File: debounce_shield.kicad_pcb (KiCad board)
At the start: 2 copper layers, 65 x 56 mm, 75 parts, among them IC1 LTV-814, IC2 LTV-814, IC3 LTV-814, IC4 LTV-814, IC5 LTV-814, IC6 LTV-814, IC7 MAX16914AUB+, J1 Conn_01x06, J2 RPi_GPIO, J3 Conn_01x06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

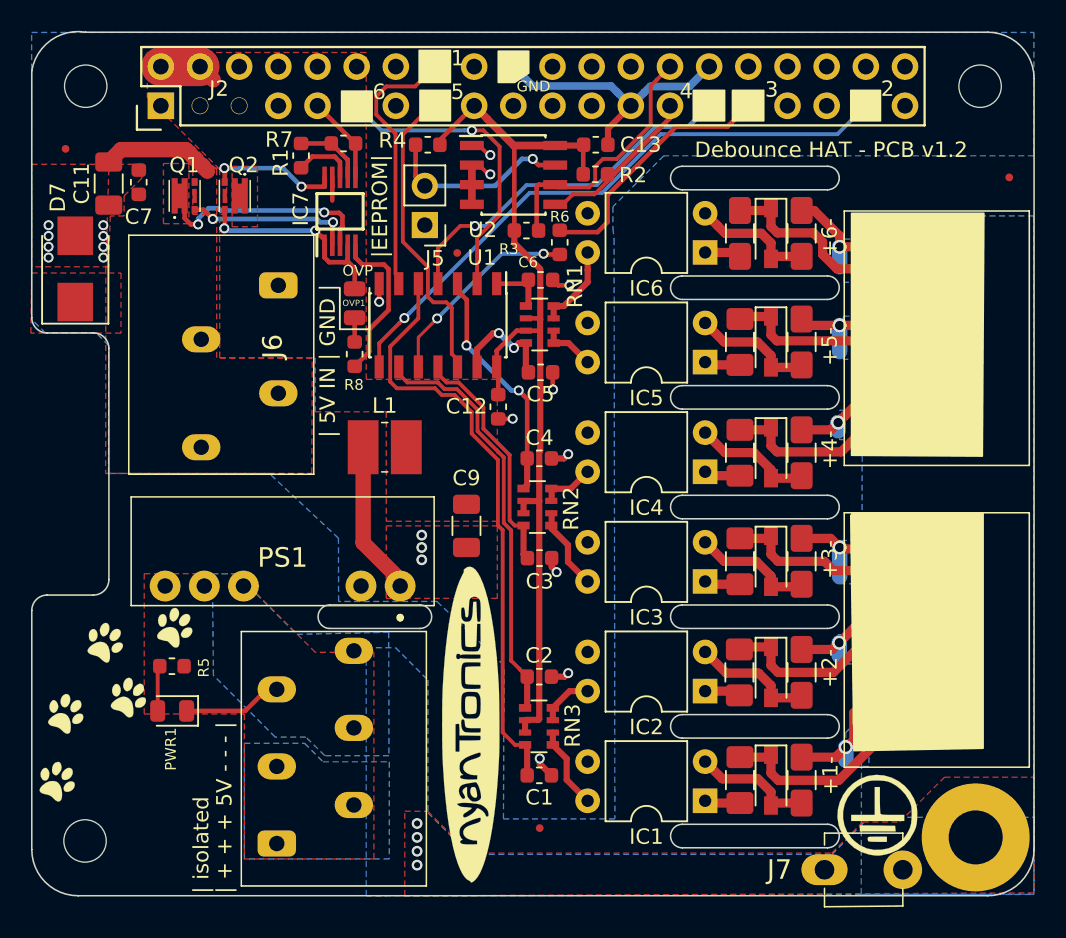
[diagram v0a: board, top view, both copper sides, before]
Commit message: Tweak isolation slots in PCB.
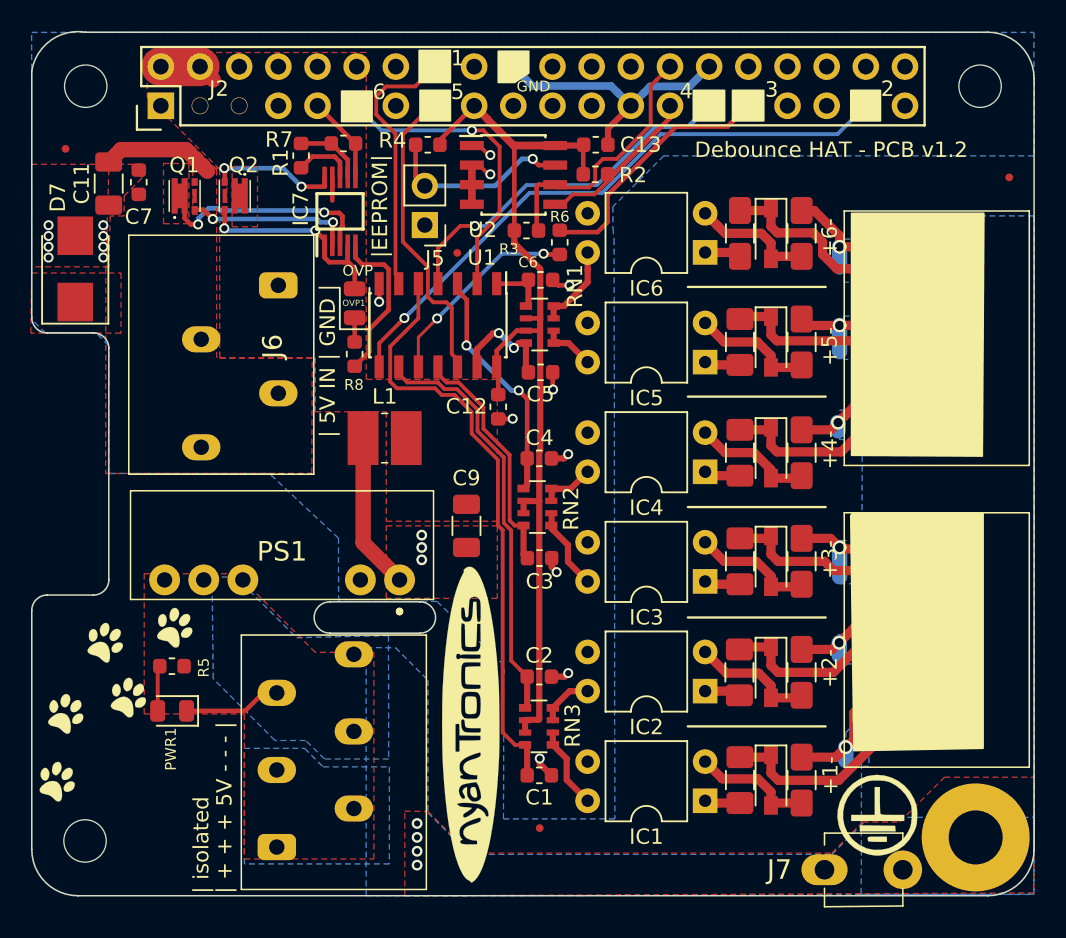
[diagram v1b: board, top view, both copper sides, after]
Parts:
- moved G*** 7.88 mm to (127.1, 103.0)
- moved L1 0.59 mm to (120.4, 98.9)
- moved PS1 0.40 mm to (121.4, 108.1)
- moved J1 0.23 mm to (118.4, 112.9)
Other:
- outline, holes or cut-outs redrawn

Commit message: Tweak isolation slots on PCB.
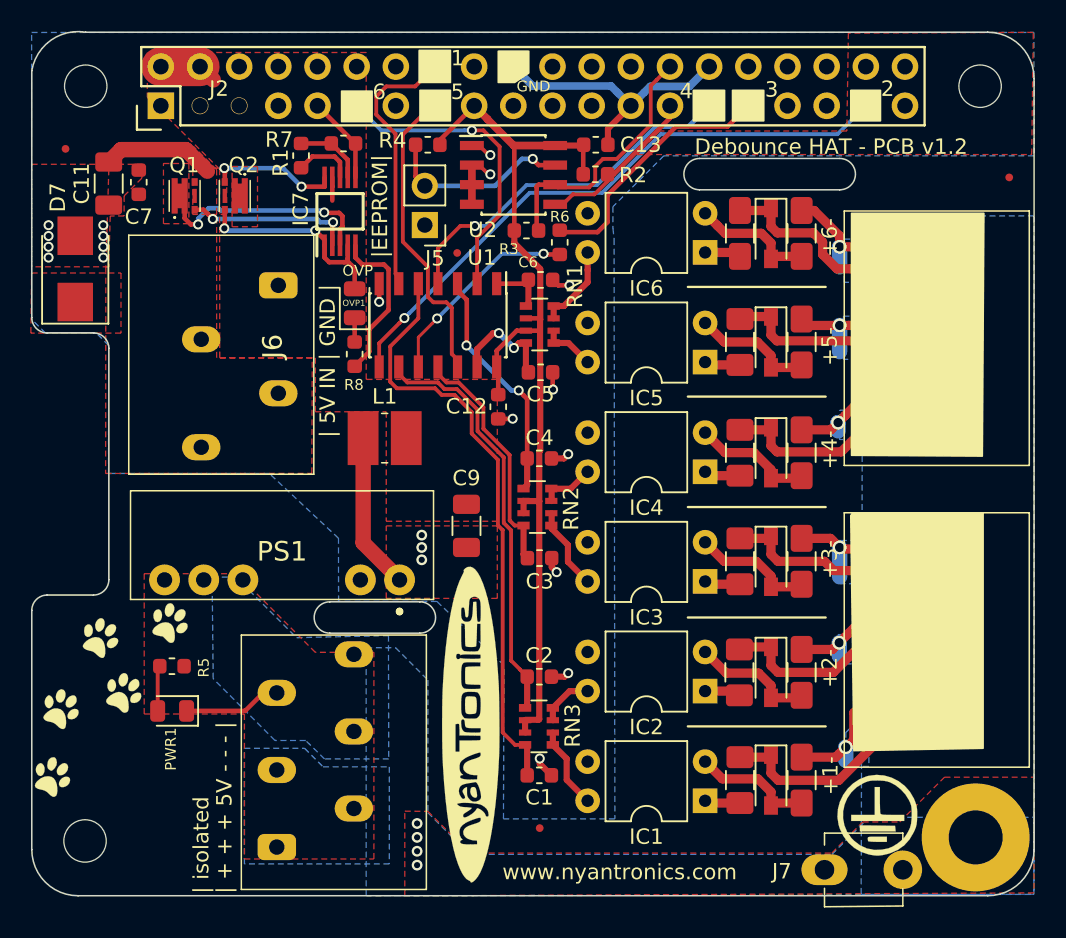
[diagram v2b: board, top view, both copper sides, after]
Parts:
- moved G*** 0.43 mm to (102.7, 115.9)
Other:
- outline, holes or cut-outs redrawn
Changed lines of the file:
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@@
   (general
     (thickness 1.6)
-    (drawings 71)
+    (drawings 75)
     (tracks 532)
     (zones 0)
@@
     (descr 1285-1)
     (tags Connector)
-    (fp_text reference J7 (at -5.46 0) (layer F.SilkS)
-      (effects (font (size 1.27 1.27) (thickness 0.254)))
+    (fp_text reference J7 (at -5.3084 0.1) (layer F.SilkS)
+      (effects (font (size 1 1) (thickness 0.15)))
     )
     (fp_text value 1285 (at 0 0.013) (layer F.SilkS) hide
@@
   )
   (module libs:kitten_paw_prints locked (layer F.Cu)
-    (at 102.9716 116.1796)
+    (at 102.6668 115.8748)
     (fp_text reference G*** (at -0.254 1.905 180) (layer F.SilkS) hide
       (effects (font (size 1.524 1.524) (thickness 0.3)))
@@
       (solder_mask_margin 0.25) (clearance 0.25))
   )
+  (gr_arc (start 149.9108 81.788) (end 149.9108 82.804) (angle -180) (layer Edge.Cuts) (width 0.1))
+  (gr_line (start 149.9108 80.772) (end 140.8176 80.772) (layer Edge.Cuts) (width 0.1))
+  (gr_line (start 149.9108 82.804) (end 140.8176 82.804) (layer Edge.Cuts) (width 0.1))
+  (gr_arc (start 140.8176 81.788) (end 140.8176 80.772) (angle -180) (layer Edge.Cuts) (width 0.1))
   (gr_line (start 148.9964 117.602) (end 140.0556 117.602) (layer F.SilkS) (width 0.15))
   (gr_line (start 148.9964 110.5408) (end 140.0556 110.5408) (layer F.SilkS) (width 0.15))
@@
     (effects (font (size 1 1) (thickness 0.2)) (justify left))
   )
-  (gr_text www.nyantronics.com (at 149.9616 80.2132) (layer B.SilkS)
-    (effects (font (size 1 1) (thickness 0.2)) (justify mirror))
+  (gr_text www.nyantronics.com (at 135.636 127.0508) (layer F.SilkS)
+    (effects (font (size 1 1) (thickness 0.2)))
   )
   (gr_text |EEPROM| (at 120.0912 83.8708 90) (layer F.SilkS)
@@
     (effects (font (size 1 1) (thickness 0.15)))
   )
-  (gr_text "Debounce HAT - PCB v1.2" (at 149.35 80.2132) (layer F.SilkS)
+  (gr_text "Debounce HAT - PCB v1.2" (at 149.35 80.01) (layer F.SilkS)
     (effects (font (size 1 1) (thickness 0.2)))
   )
@@
       )
     )
+  )
+  (zone (net 7) (net_name GND) (layer F.Cu) (hatch edge 0.508)
+    (connect_pads (clearance 0.508))
+    (min_thickness 0.254)
+    (fill yes (arc_segments 32) (thermal_gap 0.508) (thermal_bridge_width 0.508))
+    (polygon
+      (pts
+        (xy 162.3568 80.518) (xy 162.4584 72.5932) (xy 150.4696 72.644) (xy 150.368 78.994) (xy 138.2268 78.994)
+        (xy 136.7536 80.518)
+      )
+    )

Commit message: Move the paws so they don't get cut off in production.
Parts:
- moved G*** 2.02 mm to (103.5, 117.7), turned to 55 degrees
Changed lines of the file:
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@@
     (visible_elements 7FFDFFBF)
     (pcbplotparams
-      (layerselection 0x00030_80000001)
+      (layerselection 0x010fc_ffffffff)
       (usegerberextensions false)
       (usegerberattributes false)
@@
       (drillshape 0)
       (scaleselection 1)
-      (outputdirectory "meta/"))
+      (outputdirectory "gerber_v12/"))
   )
   (net 0 "")
@@
   )
   (module libs:kitten_paw_prints locked (layer F.Cu)
-    (at 102.6668 115.8748)
-    (fp_text reference G*** (at -0.254 1.905 180) (layer F.SilkS) hide
+    (at 103.5304 117.7036 55)
+    (fp_text reference G*** (at -0.254 1.905 235) (layer F.SilkS) hide
       (effects (font (size 1.524 1.524) (thickness 0.3)))
     )
-    (fp_text value LOGO (at 0.75 0 180) (layer F.SilkS) hide
+    (fp_text value LOGO (at 0.75 0 235) (layer F.SilkS) hide
       (effects (font (size 1.524 1.524) (thickness 0.3)))
     )
@@
       (solder_mask_margin 0.25) (clearance 0.25))
   )
+  (gr_poly (pts (xy 150.7744 103.7844) (xy 159.2072 103.7844) (xy 159.2072 119.1768) (xy 150.8252 119.1768)) (layer F.SilkS) (width 0.1))
   (gr_arc (start 149.9108 81.788) (end 149.9108 82.804) (angle -180) (layer Edge.Cuts) (width 0.1))
   (gr_line (start 149.9108 80.772) (end 140.8176 80.772) (layer Edge.Cuts) (width 0.1))
@@
   (gr_line (start 148.9964 96.2152) (end 140.0556 96.2152) (layer F.SilkS) (width 0.15))
   (gr_line (start 148.9964 89.1032) (end 140.0556 89.1032) (layer F.SilkS) (width 0.15))
-  (gr_poly (pts (xy 150.7236 103.7844) (xy 159.2072 103.7844) (xy 159.2072 119.0244) (xy 150.8252 119.1768) (xy 150.622 103.9368)) (layer F.SilkS) (width 0.1))
-  (gr_poly (pts (xy 159.1564 84.328) (xy 150.6728 84.328) (xy 150.6728 100.0252) (xy 159.1564 100.076) (xy 159.258 84.328)) (layer F.SilkS) (width 0.1))
+  (gr_poly (pts (xy 150.6728 84.328) (xy 150.6728 100.0252) (xy 159.1564 100.0252) (xy 159.258 84.328)) (layer F.SilkS) (width 0.1))
   (gr_text GND (at 130.048 76.0984) (layer F.SilkS)
     (effects (font (size 0.7 0.7) (thickness 0.15)))

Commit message: Update to revision 1.3.
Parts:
- moved REF** 3.40 mm to (160.8, 85.4)
- moved REF** 1.60 mm to (130.4, 122.6)
- moved G*** 0.44 mm to (103.3, 117.3)
- renumbered RN3 to RN12, RN2 to RN34, RN1 to RN56
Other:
- outline, holes or cut-outs redrawn
- board text added: "Debounce HAT - PCB v1.3"
- board text removed: "Debounce HAT - PCB v1.2"
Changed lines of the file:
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@@
   (general
     (thickness 1.6)
-    (drawings 75)
-    (tracks 532)
+    (drawings 79)
+    (tracks 533)
     (zones 0)
     (modules 75)
@@
     (visible_elements 7FFDFFBF)
     (pcbplotparams
-      (layerselection 0x010fc_ffffffff)
+      (layerselection 0x00030_80000001)
       (usegerberextensions false)
       (usegerberattributes false)
@@
       (drillshape 0)
       (scaleselection 1)
-      (outputdirectory "gerber_v12/"))
+      (outputdirectory "meta/"))
   )
   (net 0 "")
@@
     (tags "resistor array")
     (attr smd)
-    (fp_text reference RN3 (at -2.1844 0.0508 90) (layer F.SilkS)
+    (fp_text reference RN12 (at -2.1844 0.0508 90) (layer F.SilkS)
       (effects (font (size 1 1) (thickness 0.15)))
     )
@@
     (tags "resistor array")
     (attr smd)
-    (fp_text reference RN2 (at -2.1844 -0.1016 90) (layer F.SilkS)
+    (fp_text reference RN34 (at -2.1844 -0.1016 90) (layer F.SilkS)
       (effects (font (size 1 1) (thickness 0.15)))
     )
@@
     (tags "resistor array")
     (attr smd)
-    (fp_text reference RN1 (at -2.286 2.4892 90) (layer F.SilkS)
+    (fp_text reference RN56 (at -2.286 2.4892 90) (layer F.SilkS)
       (effects (font (size 1 1) (thickness 0.15)))
     )
@@
     (descr 1990041_1)
     (tags Connector)
-    (fp_text reference J4 (at -5.55 -1.3 90) (layer F.SilkS)
+    (fp_text reference J4 (at 2.2316 -2.2552 180) (layer F.SilkS)
       (effects (font (size 1.27 1.27) (thickness 0.254)))
     )
@@
     (descr 1990041_1)
     (tags Connector)
-    (fp_text reference J3 (at -5.55 -1.3 90) (layer F.SilkS)
+    (fp_text reference J3 (at 2.2704 -1.9504 180) (layer F.SilkS)
       (effects (font (size 1.27 1.27) (thickness 0.254)))
     )
@@
     (descr "4-lead though-hole mounted DIP package, row spacing 7.62 mm (300 mils)")
     (tags "THT DIP DIL PDIP 2.54mm 7.62mm 300mil")
-    (fp_text reference IC1 (at 3.81 -2.33) (layer F.SilkS)
+    (fp_text reference IC1 (at 2.178 -2.33) (layer F.SilkS)
       (effects (font (size 1 1) (thickness 0.15)))
     )
@@
   )
   (module libs:kitten_paw_prints locked (layer F.Cu)
-    (at 103.5304 117.7036 55)
+    (at 103.2764 117.348 55)
     (fp_text reference G*** (at -0.254 1.905 235) (layer F.SilkS) hide
       (effects (font (size 1.524 1.524) (thickness 0.3)))
@@
     (tags capacitor)
     (attr smd)
-    (fp_text reference C1 (at 0 -1.43 180) (layer F.SilkS)
+    (fp_text reference C1 (at 1.6252 -1.8224 180) (layer F.SilkS)
       (effects (font (size 1 1) (thickness 0.15)))
     )
@@
   )
   (module Fiducial:Fiducial_0.5mm_Dia_1mm_Outer locked (layer F.Cu)
-    (at 130.45 124.2)
+    (at 130.45 122.6)
     (descr "Circular Fiducial, 0.5mm bare copper top; 1mm keepout (Level C)")
     (tags marker)
@@
   )
   (module Fiducial:Fiducial_0.5mm_Dia_1mm_Outer locked (layer F.Cu)
-    (at 160.9 82)
+    (at 160.8 85.4)
     (descr "Circular Fiducial, 0.5mm bare copper top; 1mm keepout (Level C)")
     (tags marker)
@@
       (solder_mask_margin 0.25) (clearance 0.25))
   )
-  (gr_poly (pts (xy 150.7744 103.7844) (xy 159.2072 103.7844) (xy 159.2072 119.1768) (xy 150.8252 119.1768)) (layer F.SilkS) (width 0.1))
+  (gr_arc (start 130.4 124.588) (end 130.4 123.572) (angle -180) (layer Edge.Cuts) (width 0.1))
+  (gr_line (start 136.6 125.604) (end 130.4 125.6) (layer Edge.Cuts) (width 0.1))
+  (gr_line (start 136.6 123.572) (end 130.4 123.572) (layer Edge.Cuts) (width 0.1))
+  (gr_arc (start 136.6 124.588) (end 136.6 125.604) (angle -180) (layer Edge.Cuts) (width 0.1))
   (gr_arc (start 149.9108 81.788) (end 149.9108 82.804) (angle -180) (layer Edge.Cuts) (width 0.1))
-  (gr_line (start 149.9108 80.772) (end 140.8176 80.772) (layer Edge.Cuts) (width 0.1))
-  (gr_line (start 149.9108 82.804) (end 140.8176 82.804) (layer Edge.Cuts) (width 0.1))
-  (gr_arc (start 140.8176 81.788) (end 140.8176 80.772) (angle -180) (layer Edge.Cuts) (width 0.1))
+  (gr_line (start 149.9108 80.772) (end 139.2 80.772) (layer Edge.Cuts) (width 0.1))
+  (gr_line (start 149.9108 82.804) (end 139.2 82.804) (layer Edge.Cuts) (width 0.1))
+  (gr_arc (start 139.2 81.788) (end 139.2 80.772) (angle -180) (layer Edge.Cuts) (width 0.1))
   (gr_line (start 148.9964 117.602) (end 140.0556 117.602) (layer F.SilkS) (width 0.15))
   (gr_line (start 148.9964 110.5408) (end 140.0556 110.5408) (layer F.SilkS) (width 0.15))
@@
   (gr_line (start 148.9964 96.2152) (end 140.0556 96.2152) (layer F.SilkS) (width 0.15))
   (gr_line (start 148.9964 89.1032) (end 140.0556 89.1032) (layer F.SilkS) (width 0.15))
-  (gr_poly (pts (xy 150.6728 84.328) (xy 150.6728 100.0252) (xy 159.1564 100.0252) (xy 159.258 84.328)) (layer F.SilkS) (width 0.1))
+  (gr_poly (pts (xy 150.7236 103.7844) (xy 159.2072 103.7844) (xy 159.2072 119.0244) (xy 150.8252 119.1768) (xy 150.622 103.9368)) (layer F.SilkS) (width 0.1))
+  (gr_poly (pts (xy 159.1564 84.328) (xy 150.6728 84.328) (xy 150.6728 100.0252) (xy 159.1564 100.076) (xy 159.258 84.328)) (layer F.SilkS) (width 0.1))
   (gr_text GND (at 130.048 76.0984) (layer F.SilkS)
     (effects (font (size 0.7 0.7) (thickness 0.15)))
@@
     (effects (font (size 1 1) (thickness 0.2)) (justify left))
   )
-  (gr_arc (start 116.84 110.5408) (end 116.84 109.5248) (angle -180) (layer Edge.Cuts) (width 0.1))
-  (gr_line (start 122.682 109.5248) (end 116.84 109.5248) (layer Edge.Cuts) (width 0.1))
+  (gr_arc (start 116.2 110.5408) (end 116.2 109.5248) (angle -180) (layer Edge.Cuts) (width 0.1))
+  (gr_line (start 122.682 109.5248) (end 116.2 109.5248) (layer Edge.Cuts) (width 0.1))
   (gr_arc (start 122.682 110.5408) (end 122.682 111.5568) (angle -180) (layer Edge.Cuts) (width 0.1))
-  (gr_line (start 116.84 111.5568) (end 122.682 111.5568) (layer Edge.Cuts) (width 0.1))
+  (gr_line (start 116.2 111.5568) (end 122.682 111.5568) (layer Edge.Cuts) (width 0.1))
   (gr_poly (pts (xy 152.623327 86.300017) (xy 154.8 84.1) (xy 157.4 84.1) (xy 157.4 117) (xy 155 119.4) (xy 152.6 119.4)) (layer B.Mask) (width 0.1))
   (gr_text PE (at 151.6 126.65 90) (layer B.SilkS)
@@
     (effects (font (size 1 1) (thickness 0.2)))
   )
-  (gr_text "| 5V IN | GND |\n" (at 116.7 93.9 90) (layer F.SilkS)
+  (gr_text "| 5V IN | GND |\n" (at 116.7 94.6 90) (layer F.SilkS)
     (effects (font (size 1 1) (thickness 0.2)))
   )
@@
     (effects (font (size 1 1) (thickness 0.15)))
   )
-  (gr_text "Debounce HAT - PCB v1.2" (at 149.35 80.01) (layer F.SilkS)
+  (gr_text "Debounce HAT - PCB v1.3" (at 149.35 80.01) (layer F.SilkS)
     (effects (font (size 1 1) (thickness 0.2)))
   )
@@
   (segment (start 122.9995 82.55) (end 127.55 82.55) (width 0.3) (layer B.Cu) (net 40))
   (segment (start 127.55 82.55) (end 129.3 80.8) (width 0.3) (layer B.Cu) (net 40))
-  (segment (start 121.4 108.1) (end 121.4 108.5) (width 1) (layer F.Cu) (net 41))
-  (segment (start 119 99.5) (end 119 105.7) (width 1) (layer F.Cu) (net 41))
-  (segment (start 119 105.7) (end 121.4 108.1) (width 1) (layer F.Cu) (net 41))
+  (segment (start 121.4 107.4) (end 121.4 108.5) (width 1) (layer F.Cu) (net 41))
+  (segment (start 119.8 105.8) (end 121.4 107.4) (width 1) (layer F.Cu) (net 41))
+  (segment (start 119 99.5) (end 119.8 100.3) (width 1) (layer F.Cu) (net 41))
+  (segment (start 119.8 100.3) (end 119.8 105.8) (width 1) (layer F.Cu) (net 41))
   (segment (start 147.2735 115.75) (end 147.436 115.5875) (width 0.6) (layer F.Cu) (net 43) (status 30))
   (segment (start 145.45 115.75) (end 147.2735 115.75) (width 0.6) (layer F.Cu) (net 43) (status 30))
@@
       (pts
         (xy 162.5 72.6) (xy 162.5 80.6) (xy 138.5 80.6) (xy 135.2 83.9) (xy 135.2 85.3)
-        (xy 135.275 86) (xy 135.325 123.6) (xy 128.1 123.6) (xy 128.135807 113.635807) (xy 123.782737 109.5)
-        (xy 117.408632 109.5) (xy 117.4 105.4) (xy 112.913044 101.2) (xy 102.486957 101.2) (xy 102.5 92.9)
-        (xy 101.7 92.1) (xy 98.4 92.1) (xy 97.5 91.2) (xy 97.5 72.6)
+        (xy 135.275 86) (xy 135.325 123.8) (xy 132.8 123.8) (xy 128.2 119.2) (xy 128.135807 113.635807)
+        (xy 123.782737 109.5) (xy 117.408632 109.5) (xy 117.4 105.4) (xy 112.913044 101.2) (xy 102.486957 101.2)
+        (xy 102.5 92.9) (xy 101.7 92.1) (xy 98.4 92.1) (xy 97.5 91.2) (xy 97.5 72.6)
       )
     )
